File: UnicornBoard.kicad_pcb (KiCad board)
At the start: 2 copper layers, 48.1 x 58.1 mm, 41 parts, among them U1 ATSAMD21E18A-AU, U2 AP2112K-3.3

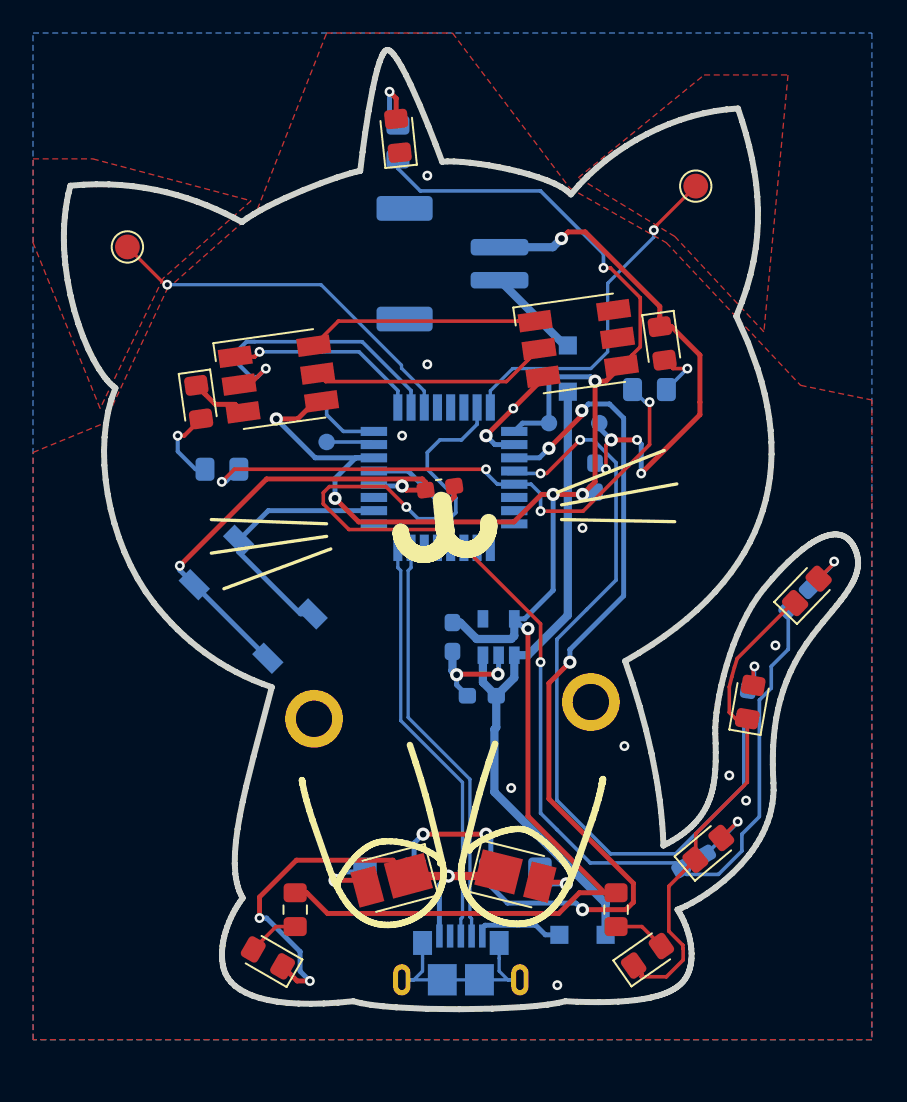
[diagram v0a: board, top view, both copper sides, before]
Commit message: Version 2, new outline
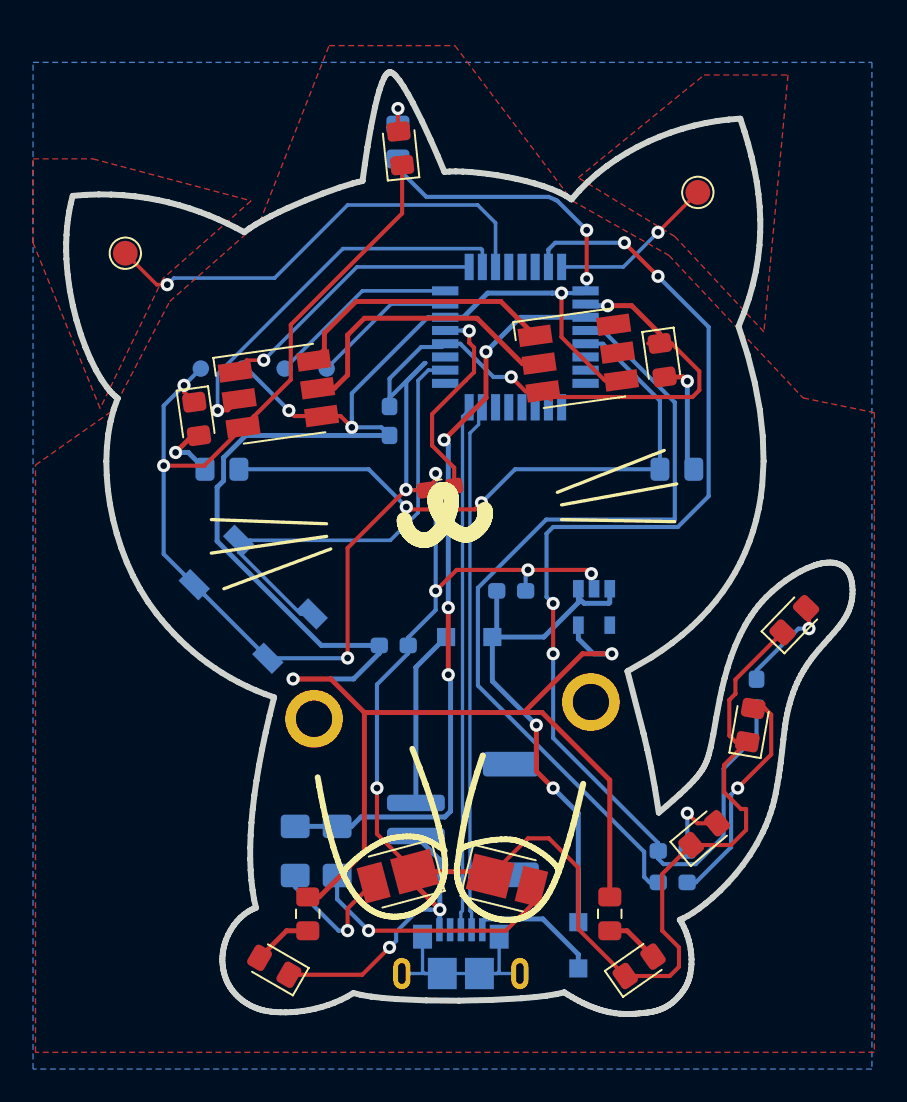
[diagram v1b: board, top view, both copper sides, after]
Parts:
- moved BT1 33.7 mm to (229.2, 141.6), turned to 270 degrees
- moved GND 24.4 mm to (213.4, 114.3)
- moved 3V3 18.8 mm to (215.9, 114.3)
- moved D50 17.3 mm to (229.6, 130.6), turned to 180 degrees
- moved C4 12.9 mm to (224.8, 117.5)
- moved R6 11.7 mm to (241.9, 145.4), turned to 0 degrees
- moved R3 10.9 mm to (221.6, 143.5), turned to 90 degrees
- moved U1 9.54 mm to (232.4, 112.4)
- moved C3 6.59 mm to (232.2, 127.8), turned to 0 degrees
- moved R5 6.25 mm to (247.0, 134.0), turned to 90 degrees
- moved U2 6.06 mm to (237.2, 128.7), turned to 270 degrees
- moved R2 5.85 mm to (219.1, 143.5), turned to 90 degrees
- moved R0 5.10 mm to (242.2, 120.4)
- moved 31 4.45 mm to (221.0, 114.3)
- moved C2 3.59 mm to (225.0, 131.1), turned to 180 degrees
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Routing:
- net GND: track 137.9 -> 222.8 mm, vias 24 -> 13
- net Net-(R2-Pad2): track 60.8 -> 45.7 mm, vias 6 -> 4
- net +3V3: track 125.3 -> 140.4 mm
- net Net-(SW1-Pad1): track 15.6 -> 28.2 mm
- net Net-(D3-Pad2): track 3.55 -> 15.8 mm
- net Net-(Touch1-Pad1): track 21.3 -> 10.1 mm
- net Net-(D6-Pad2): track 2.76 -> 13.8 mm
- net Net-(C3-Pad1): track 40.8 -> 32.7 mm, vias 0 -> 2
- net Net-(J32-Pad1): track 4.17 -> 11.7 mm
- net /USB_D-: track 25.2 -> 32.0 mm
- net Net-(R4-Pad1): track 76.6 -> 69.9 mm, vias 2 -> 4
- net /USB_D+: track 25.2 -> 31.8 mm
- net Net-(C1-Pad2): track 6.67 -> 12.7 mm
- net Net-(J31-Pad1): track 2.93 -> 8.80 mm
- net Net-(Touch2-Pad1): track 22.7 -> 28.3 mm
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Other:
- board size 48.1 x 58.1 mm -> 47.6 x 57 mm

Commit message: Minor silk revision
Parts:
- micro USB: renamed from USB
- renumbered BT1 to Batt+
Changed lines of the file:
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@@
   )
   (layers
-    (0 F.Cu signal)
-    (31 B.Cu signal hide)
+    (0 F.Cu signal hide)
+    (31 B.Cu signal)
     (32 B.Adhes user hide)
     (33 F.Adhes user hide)
     (34 B.Paste user hide)
     (35 F.Paste user hide)
-    (36 B.SilkS user hide)
+    (36 B.SilkS user)
     (37 F.SilkS user hide)
     (38 B.Mask user hide)
-    (39 F.Mask user)
+    (39 F.Mask user hide)
     (40 Dwgs.User user hide)
     (41 Cmts.User user hide)
@@
     (tags "connector JST PH top entry")
     (attr smd)
-    (fp_text reference BT1 (at 0 5.8 90) (layer B.SilkS)
+    (fp_text reference Batt+ (at -4.445 4.191 90) (layer B.SilkS)
       (effects (font (size 1 1) (thickness 0.15)) (justify mirror))
     )
@@
     (tags "Micro-USB SMD Typ-B GCT")
     (attr smd)
-    (fp_text reference USB (at 0 3.3) (layer B.SilkS)
+    (fp_text reference "micro USB" (at 0 3.175) (layer B.SilkS)
       (effects (font (size 1 1) (thickness 0.15)) (justify mirror))
     )
@@
     (tags D_SOD-123F)
     (attr smd)
-    (fp_text reference D50 (at -0.127 1.905) (layer B.SilkS)
+    (fp_text reference D50 (at -0.508 -2.032) (layer B.SilkS)
       (effects (font (size 1 1) (thickness 0.15)) (justify mirror))
     )
@@
     (tags "resistor handsolder")
     (attr smd)
-    (fp_text reference R8 (at 3.302 -0.254 90) (layer B.SilkS)
+    (fp_text reference R8 (at -2.54 0.508 180) (layer B.SilkS)
       (effects (font (size 1 1) (thickness 0.15)) (justify mirror))
     )
@@
     (tags "test point SMD pad")
     (attr virtual)
-    (fp_text reference 3V3 (at 0 2.54) (layer B.SilkS)
+    (fp_text reference 3V3 (at 0 1.524) (layer B.SilkS)
       (effects (font (size 1 1) (thickness 0.15)) (justify mirror))
     )
@@
     (tags "test point SMD pad")
     (attr virtual)
-    (fp_text reference 32 (at 0 2.54) (layer B.SilkS)
+    (fp_text reference 32 (at 0 1.524) (layer B.SilkS)
       (effects (font (size 1 1) (thickness 0.15)) (justify mirror))
     )
@@
     (tags "test point SMD pad")
     (attr virtual)
-    (fp_text reference 31 (at 0 -2.54) (layer B.SilkS)
-      (effects (font (size 1 1) (thickness 0.15)) (justify mirror))
-    )
+    (fp_text reference 31 (at 0 -1.524) (layer B.SilkS)
+      (effects (font (size 1 1) (thickness 0.15)) (justify mirror))
+    )
